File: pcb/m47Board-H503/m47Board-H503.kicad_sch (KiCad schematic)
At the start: 22 parts, among them J1 USB_C_Receptacle_USB2.0_14P, SW1 SW_Push, SW2 SW_Push, U1 STM32H503CBTx, Y1 16MHz, Y2 Crystal_GND24

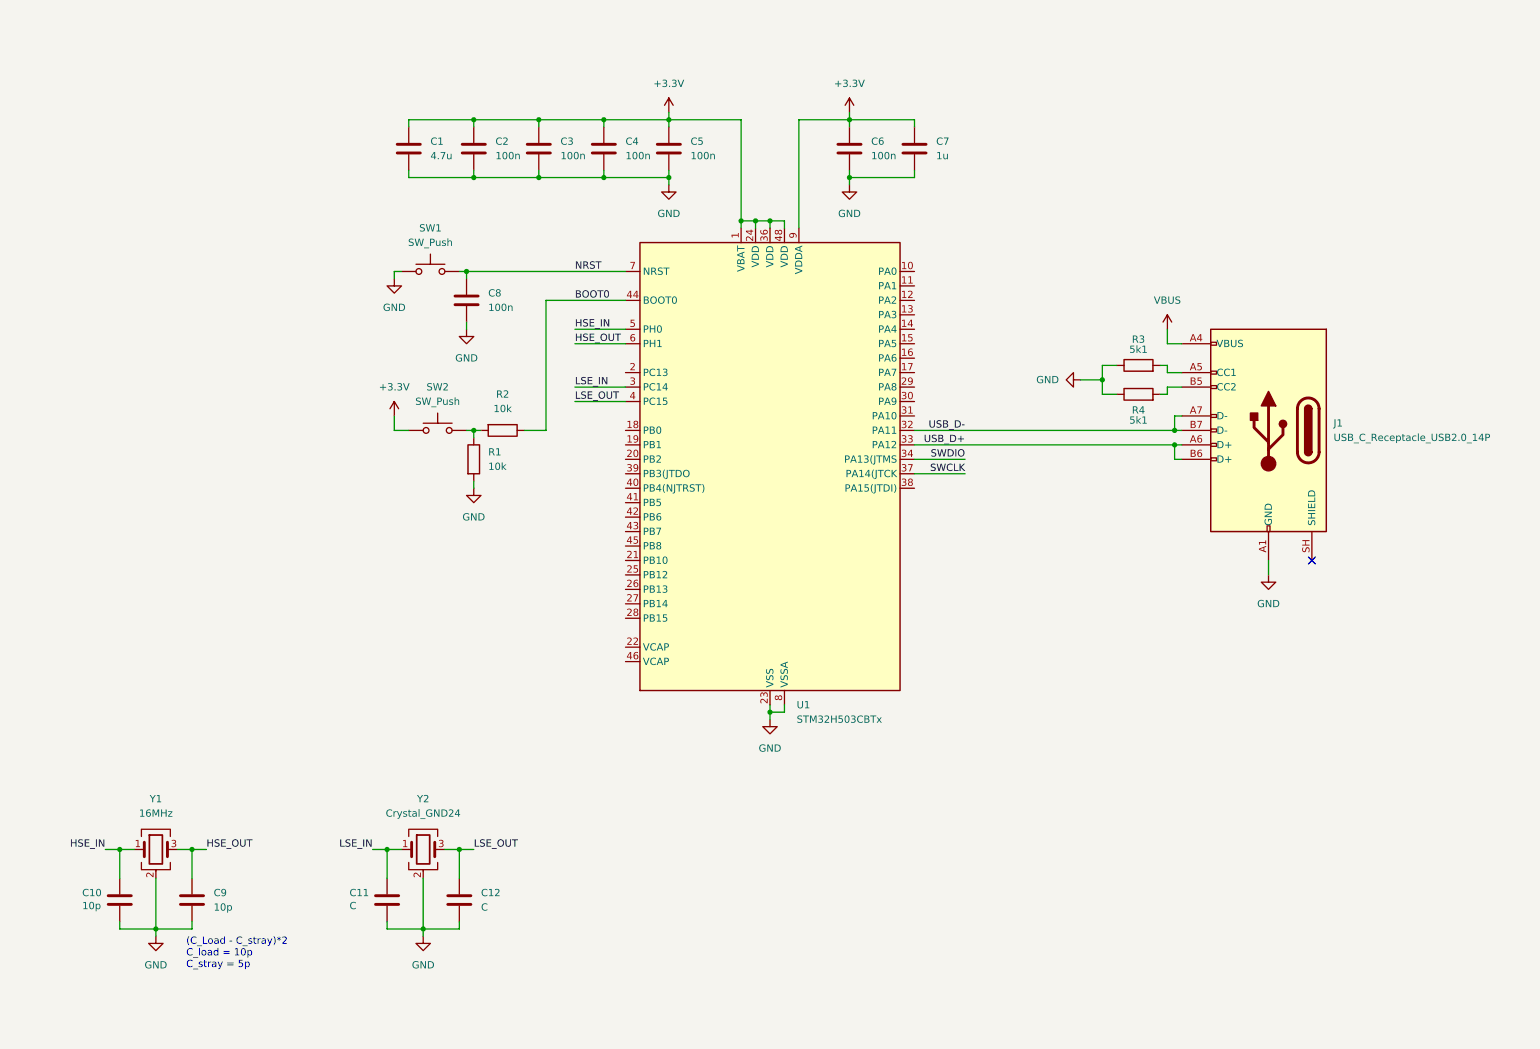
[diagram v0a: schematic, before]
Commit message: Update m47Board-H503 schematic
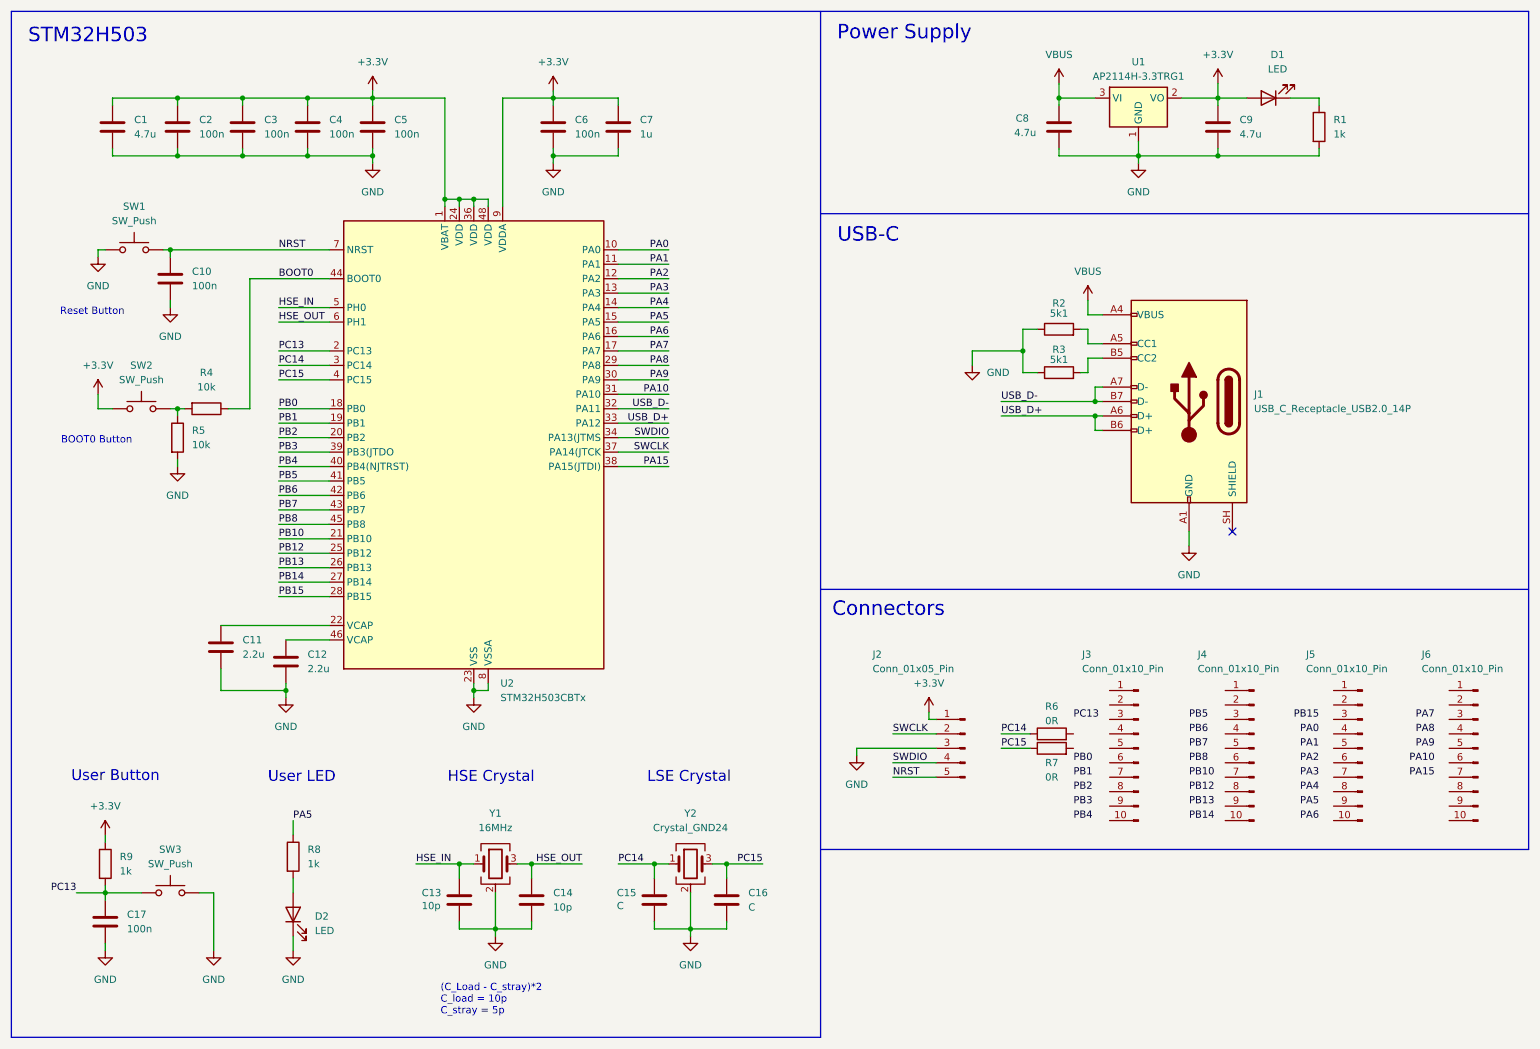
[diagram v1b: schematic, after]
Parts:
- added C11, C12: 2.2u, symbol Device:C
- added C17: 100n, symbol Device:C
- added C8, C9: 4.7u, symbol Device:C
- added D1, D2: LED, symbol Device:LED
- added J2: Conn_01x05_Pin, symbol Connector:Conn_01x05_Pin
- added J3, J4, J5, J6: Conn_01x10_Pin, symbol Connector:Conn_01x10_Pin
- added R1, R8, R9: 1k, symbol Device:R
- added R6, R7: 0R, symbol Device:R
- added SW3: SW_Push, symbol Switch:SW_Push
- added U1: AP2114H-3.3TRG1, Package_TO_SOT_SMD:SOT-223-3_TabPin2, symbol mc_custom_symbols:AP2114H-3.3TRG1
- renumbered C8 to C10, C10 to C13, C9 to C14, C11 to C15, C12 to C16, R3 to R2, R4 to R3, R2 to R4, R1 to R5, U1 to U2
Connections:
- net +3.3V: now also C9.1, D1.2 (A), J2.1 (Pin_1), R9.1, U1.2 (VO)
- net GND: now also C11.2, C12.2, C17.2, C8.2, C9.2, D2.1 (K), J2.3 (Pin_3), R1.2, SW3.2, U1.1 (GND)
- net NRST: now also J2.5 (Pin_5)
- net SWCLK: now also J2.2 (Pin_2)
- net SWDIO: now also J2.4 (Pin_4)
- net VBUS: now also C8.1, U1.3 (VI)
- net PA0: now reaches U2.10 (PA0)
- net PA1: now reaches U2.11 (PA1)
- net PA2: now reaches U2.12 (PA2)
- net PA3: now reaches U2.13 (PA3)
- net PA4: now reaches U2.14 (PA4)
- net PA5: now reaches U2.15 (PA5)
- net PA5: now also R8.1
- net PA6: now reaches U2.16 (PA6)
- net PA7: now reaches U2.17 (PA7)
- net PB0: now reaches U2.18 (PB0)
- net PB1: now reaches U2.19 (PB1)
- net PC13: now reaches U2.2 (PC13)
- net PC13: now also C17.1, R9.2, SW3.1
- net PB2: now reaches U2.20 (PB2)
- net PB10: now reaches U2.21 (PB10)
- net at U2.22 (VCAP): now also C11.1
- net PB12: now reaches U2.25 (PB12)
- net PB13: now reaches U2.26 (PB13)
- net PB14: now reaches U2.27 (PB14)
- net PB15: now reaches U2.28 (PB15)
- net PA8: now reaches U2.29 (PA8)
- net PA9: now reaches U2.30 (PA9)
- net PA10: now reaches U2.31 (PA10)
- net PA15: now reaches U2.38 (PA15(JTDI))
- net PB3: now reaches U2.39 (PB3(JTDO)
- net PB4: now reaches U2.40 (PB4(NJTRST))
- net PB5: now reaches U2.41 (PB5)
- net PB6: now reaches U2.42 (PB6)
- net PB7: now reaches U2.43 (PB7)
- net PB8: now reaches U2.45 (PB8)
- net at U2.46 (VCAP): now also C12.1
- net LSE_IN renamed PC14
- net PC14: now also R6.1
- net LSE_OUT renamed PC15
- net PC15: now also R7.1
- new net: D1.1 (K), R1.1
- new net: D2.2 (A), R8.2
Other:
- note added: "BOOT0 Button"
- note added: "Connectors"
- note added: "HSE Crystal"
- note added: "LSE Crystal"
- note added: "Power Supply"
- note added: "Reset Button"
- note added: "STM32H503"
- note added: "USB-C"
- note added: "User Button"
- note added: "User LED"
- company: (none) -> m47eus2
- title: (none) -> m47Board-H503
- moved on the sheet: C1, C10, C13, C14, C15, C16, C2, C3, C4, C5, C6, C7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
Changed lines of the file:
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@@
 	(generator_version "10.0")
 	(paper "A4")
+	(title_block
+		(title "m47Board-H503")
+		(date "2026-04-28")
+		(rev "0.1")
+		(company "m47eus2")
+	)
